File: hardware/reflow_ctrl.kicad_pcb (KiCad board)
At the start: 2 copper layers, 22 parts, among them IC1 MAX6675, U2 MOC3063, U3 BTA41/600B, X1 Master, X2 Mains, X3 Load, X4 Thermocouple

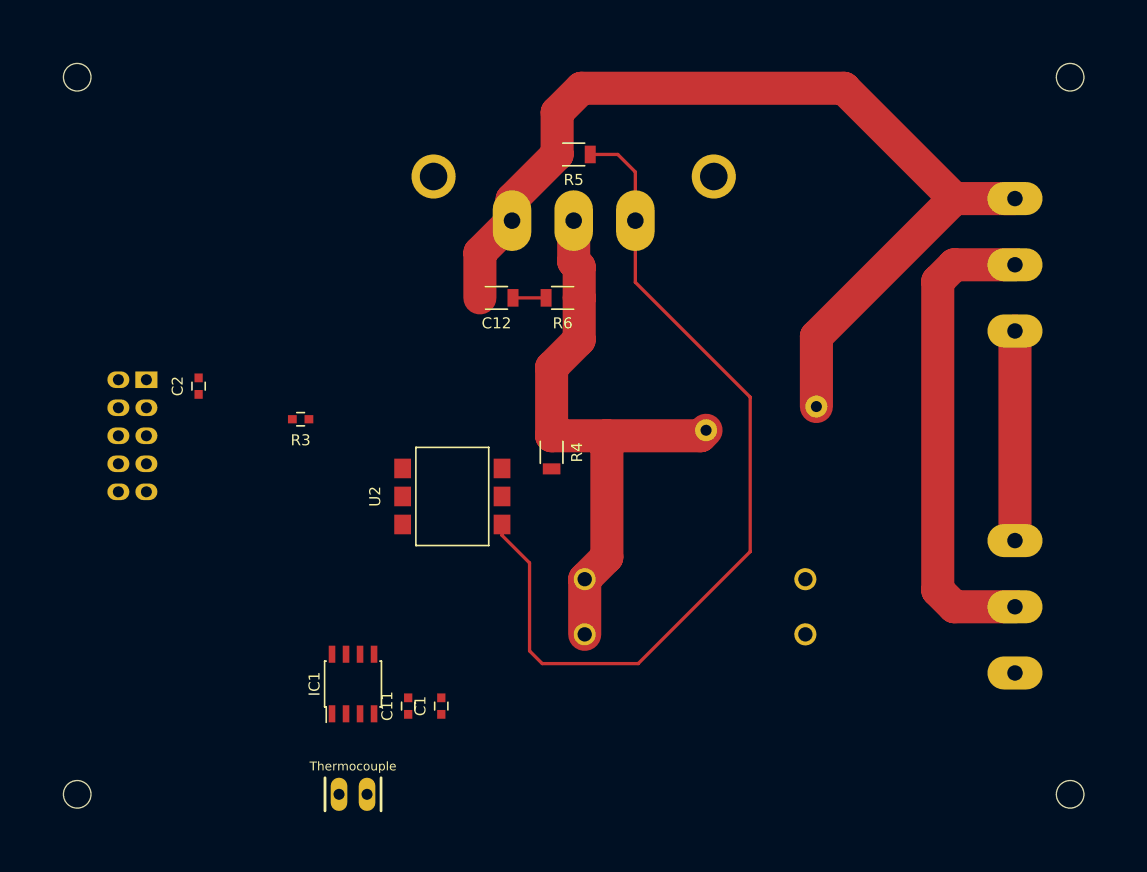
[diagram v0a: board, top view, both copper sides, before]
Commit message: Revise placement; Route
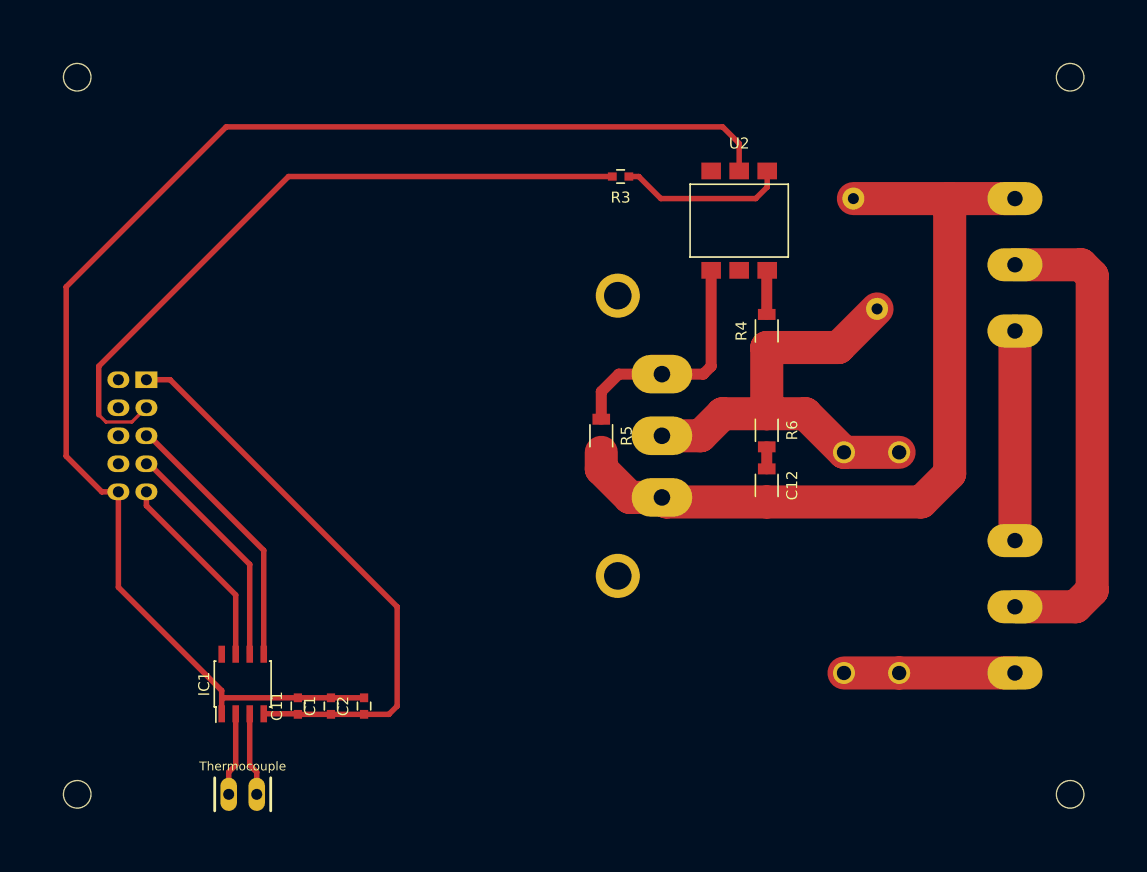
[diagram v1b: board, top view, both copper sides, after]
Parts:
- moved R3 36.4 mm to (154.2, 64.0)
- moved U2 36.1 mm to (165.0, 68.0), turned to 180 degrees
- moved C2 32.6 mm to (131.0, 112.0)
- moved C12 29.8 mm to (167.5, 92.0), turned to 270 degrees
- moved R5 25.6 mm to (152.5, 87.5), turned to 270 degrees
- moved HS1 23.8 mm to (154.0, 87.5), turned to 90 degrees
- moved R4 22.4 mm to (167.5, 78.0), turned to 90 degrees
- moved R6 22.1 mm to (167.5, 87.0), turned to 270 degrees
- moved U3 21.1 mm to (158.0, 87.5), turned to 90 degrees
- moved VR1 19.0 mm to (177.5, 76.0), turned to 90 degrees
- moved F1 16.5 mm to (177.0, 99.0), turned to 270 degrees
- moved C1 10.0 mm to (128.0, 112.0)
- moved C11 10.0 mm to (125.0, 112.0)
- moved IC1 10.0 mm to (120.0, 110.0)
- moved X4 10.0 mm to (120.0, 120.0)
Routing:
- net GND: track 0.00 -> 128.5 mm
- net /PWR: track 0.00 -> 63.2 mm
- net /MOC_A2: track 80.6 -> 22.1 mm
- net +3V3: track 0.00 -> 52.7 mm
- net /TC_SCK: track 0.00 -> 24.3 mm
- net /~TC_CS: track 0.00 -> 21.3 mm
- net /TC_SO: track 0.00 -> 18.1 mm
- net /L_mains: track 0.00 -> 15.5 mm
- net /L_load: track 90.3 -> 75.0 mm
- net Net-(R3-Pad1): track 0.00 -> 15.3 mm
- net /L_main_fused: track 53.8 -> 41.2 mm
- net /TC-: track 0.00 -> 7.56 mm
- net /TC+: track 0.00 -> 7.56 mm
- net /MOC_A1: track 0.00 -> 4.01 mm
- net /Snub: track 3.00 -> 2.00 mm
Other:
- net class AC-LC: trace_width 0.3 -> 1

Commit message: Finish routing
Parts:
- X4: moved to B.Cu
- moved R3 23.8 mm to (130.5, 64.0)
- moved U2 22.5 mm to (142.5, 66.5), turned to 270 degrees
- moved C12 4.12 mm to (163.5, 93.0)
- moved R6 4.12 mm to (163.5, 88.0)
- moved F1 4.00 mm to (173.0, 99.0)
- moved HS1 4.00 mm to (150.0, 87.5)
- moved R4 4.00 mm to (163.5, 78.0)
- moved R5 4.00 mm to (148.5, 87.5)
- moved U3 4.00 mm to (154.0, 87.5)
- moved VR1 4.00 mm to (173.5, 76.0)
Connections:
- HS1 pad 1: (no net) -> /PE_mains
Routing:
- net /PWR: track 63.2 -> 39.4 mm
- net GND: track 128.5 -> 108.0 mm
- net /MOC_A1: track 4.01 -> 22.6 mm
- net /L_mains: track 15.5 -> 34.0 mm
- net /L_load: track 75.0 -> 93.0 mm
- net Net-(R3-Pad1): track 15.3 -> 6.76 mm
- net /L_main_fused: track 41.2 -> 48.3 mm
- net /MOC_A2: track 22.1 -> 27.5 mm
- net /~TC_CS: track 21.3 -> 22.8 mm
- net /TC_SO: track 18.1 -> 19.4 mm
- net /TC_SCK: track 24.3 -> 25.5 mm
- added copper zone on F.Cu, net /PE_mains
- added copper zone on F.Cu, net GND

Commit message: Edit optotriac package; DRC clean
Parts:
- U2: footprint uMIDI:MOC3063_SMT -> uMIDI:Semi-Optotriac_MOC3063-SMD
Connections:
- HS1 pad 1: /PE_mains -> (no net)
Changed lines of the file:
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@@
 (kicad_pcb (version 4) (host pcbnew "(2015-09-12 BZR 6188)-product")
   (general
-    (links 35)
+    (links 33)
     (no_connects 0)
     (area 95.615476 49.075 213 132.700001)
@@
     )
   )
-  (module uMIDI:MOC3063_SMT (layer F.Cu)
-    (at 142.5 66.5 270)
-    (fp_text reference U2 (at 0 7 270) (layer F.SilkS)
-      (effects (font (size 1 1) (thickness 0.15)))
-    )
-    (fp_text value MOC3063 (at 0 -7 270) (layer F.Fab)
-      (effects (font (size 1 1) (thickness 0.15)))
-    )
-    (fp_line (start 4.45 -3.3) (end -4.45 -3.3) (layer F.SilkS) (width 0.15))
-    (fp_line (start 4.45 3.3) (end 4.45 -3.3) (layer F.SilkS) (width 0.15))
-    (fp_line (start -4.45 3.3) (end -4.45 -3.3) (layer F.SilkS) (width 0.15))
-    (fp_line (start 4.45 3.3) (end -4.45 3.3) (layer F.SilkS) (width 0.15))
-    (pad 2 smd trapezoid (at 0 4.505 270) (size 1.78 1.52) (layers F.Cu F.Paste F.Mask)
-      (net 1 GND))
-    (pad 1 smd trapezoid (at -2.54 4.505 270) (size 1.78 1.52) (layers F.Cu F.Paste F.Mask)
-      (net 7 "Net-(R3-Pad1)"))
-    (pad 3 smd trapezoid (at 2.54 4.505 270) (size 1.78 1.52) (layers F.Cu F.Paste F.Mask))
-    (pad 6 smd trapezoid (at -2.54 -4.505 270) (size 1.78 1.52) (layers F.Cu F.Paste F.Mask)
-      (net 15 /MOC_A1))
-    (pad 5 smd trapezoid (at 0 -4.505 270) (size 1.78 1.52) (layers F.Cu F.Paste F.Mask))
-    (pad 4 smd trapezoid (at 2.54 -4.505 270) (size 1.78 1.52) (layers F.Cu F.Paste F.Mask)
-      (net 16 /MOC_A2))
-  )
   (module TO_SOT_Packages_THT:TO-247_Vertical_Neutral123_largePads locked (layer B.Cu)
     (at 154 87.5 90)
@@
     (fp_line (start 1.6 -0.7) (end 1.6 -0.9) (layer B.SilkS) (width 0.15))
     (pad 1 thru_hole circle (at -12.7 0 90) (size 4 4) (drill 2.5) (layers *.Cu *.Mask)
-      (net 8 /PE_mains) (zone_connect 2))
+      (zone_connect 2))
     (pad 1 thru_hole circle (at 12.7 0 90) (size 4 4) (drill 2.5) (layers *.Cu *.Mask)
-      (net 8 /PE_mains) (zone_connect 2))
+      (zone_connect 2))
+  )
+  (module uMIDI:Semi-Optotriac_MOC3063-SMD (layer F.Cu)
+    (at 142.5 66.5 270)
+    (fp_text reference U2 (at 0 7 270) (layer F.SilkS)
+      (effects (font (size 1 1) (thickness 0.15)))
+    )
+    (fp_text value MOC3063 (at 0 -7 270) (layer F.Fab)
+      (effects (font (size 1 1) (thickness 0.15)))
+    )
+    (fp_circle (center -3 2) (end -2.3 2) (layer F.SilkS) (width 0.15))
+    (fp_line (start 4.45 -3.3) (end -4.45 -3.3) (layer F.SilkS) (width 0.15))
+    (fp_line (start 4.45 3.3) (end 4.45 -3.3) (layer F.SilkS) (width 0.15))
+    (fp_line (start -4.45 3.3) (end -4.45 -3.3) (layer F.SilkS) (width 0.15))
+    (fp_line (start 4.45 3.3) (end -4.45 3.3) (layer F.SilkS) (width 0.15))
+    (pad 2 smd trapezoid (at 0 4.505 270) (size 1.78 1.52) (layers F.Cu F.Paste F.Mask)
+      (net 1 GND))
+    (pad 1 smd trapezoid (at -2.54 4.505 270) (size 1.78 1.52) (layers F.Cu F.Paste F.Mask)
+      (net 7 "Net-(R3-Pad1)"))
+    (pad 3 smd trapezoid (at 2.54 4.505 270) (size 1.78 1.52) (layers F.Cu F.Paste F.Mask))
+    (pad 6 smd trapezoid (at -2.54 -4.505 270) (size 1.78 1.52) (layers F.Cu F.Paste F.Mask)
+      (net 15 /MOC_A1))
+    (pad 5 smd trapezoid (at 0 -4.505 270) (size 1 1.52) (layers F.Cu F.Paste F.Mask))
+    (pad 4 smd trapezoid (at 2.54 -4.505 270) (size 1.78 1.52) (layers F.Cu F.Paste F.Mask)
+      (net 16 /MOC_A2))
   )
   (gr_line (start 150 125) (end 150 50) (layer Dwgs.User) (width 0.15))
@@
   (segment (start 172.650147 83) (end 173.5 83.849853) (width 5) (layer F.Cu) (net 17))
   (segment (start 157.5 87.5) (end 162 83) (width 5) (layer F.Cu) (net 17))
-  (segment (start 154 87.5) (end 157.5 87.5) (width 3) (layer F.Cu) (net 17))
+  (segment (start 154 87.5) (end 157.5 87.5) (width 4) (layer F.Cu) (net 17))
   (segment (start 173.5 76) (end 173.5 83.849853) (width 5) (layer F.Cu) (net 17))
   (segment (start 173.5 83.849853) (end 173.5 88.505825) (width 5) (layer F.Cu) (net 17))

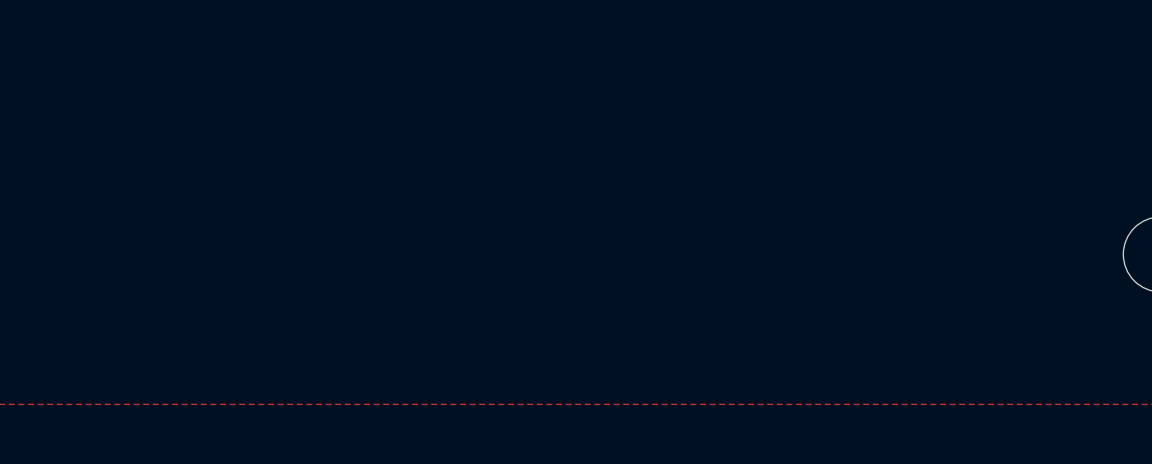
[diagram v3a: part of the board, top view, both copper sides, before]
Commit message: Connect heatsink to PE
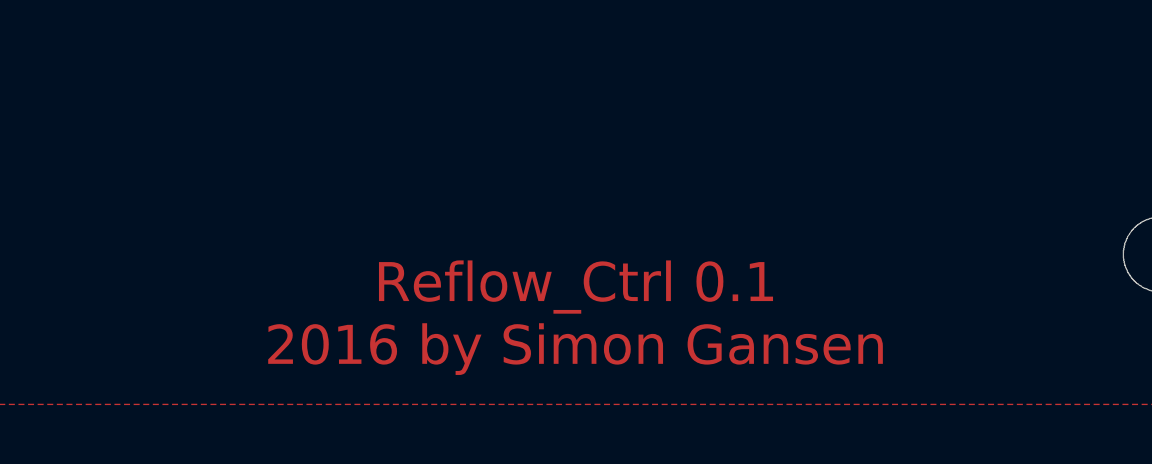
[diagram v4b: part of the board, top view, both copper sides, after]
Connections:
- HS1 pad 1: (no net) -> /PE_mains
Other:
- board text added: "Reflow_Ctrl 0.1 2016 by Simon Gansen"
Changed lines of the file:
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@@
 (kicad_pcb (version 4) (host pcbnew "(2015-09-12 BZR 6188)-product")
   (general
-    (links 33)
+    (links 35)
     (no_connects 0)
     (area 95.615476 49.075 213 132.700001)
     (thickness 1.6)
-    (drawings 8)
+    (drawings 9)
     (tracks 111)
     (zones 0)
@@
   )
   (setup
-    (last_trace_width 0.5)
+    (last_trace_width 0.3)
     (user_trace_width 0.5)
     (user_trace_width 1)
@@
     (mod_text_size 1 1)
     (mod_text_width 0.15)
-    (pad_size 3 5)
-    (pad_drill 1.4)
+    (pad_size 4 4)
+    (pad_drill 2.5)
     (pad_to_mask_clearance 0.2)
     (aux_axis_origin 0 0)
@@
     (fp_line (start 1.6 -0.7) (end 1.6 -0.9) (layer B.SilkS) (width 0.15))
     (pad 1 thru_hole circle (at -12.7 0 90) (size 4 4) (drill 2.5) (layers *.Cu *.Mask)
-      (zone_connect 2))
+      (net 8 /PE_mains) (zone_connect 2))
     (pad 1 thru_hole circle (at 12.7 0 90) (size 4 4) (drill 2.5) (layers *.Cu *.Mask)
-      (zone_connect 2))
+      (net 8 /PE_mains) (zone_connect 2))
   )
   (module uMIDI:Semi-Optotriac_MOC3063-SMD (layer F.Cu)
@@
       (net 16 /MOC_A2))
   )
+  (gr_text "Reflow_Ctrl 0.1\n2016 by Simon Gansen" (at 175.5 122) (layer F.Cu)
+    (effects (font (size 1.3 1.3) (thickness 0.3)))
+  )
   (gr_line (start 150 125) (end 150 50) (layer Dwgs.User) (width 0.15))
